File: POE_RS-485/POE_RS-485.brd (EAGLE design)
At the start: 44.5 x 38.1 mm, 9 parts, among them IC1 7805

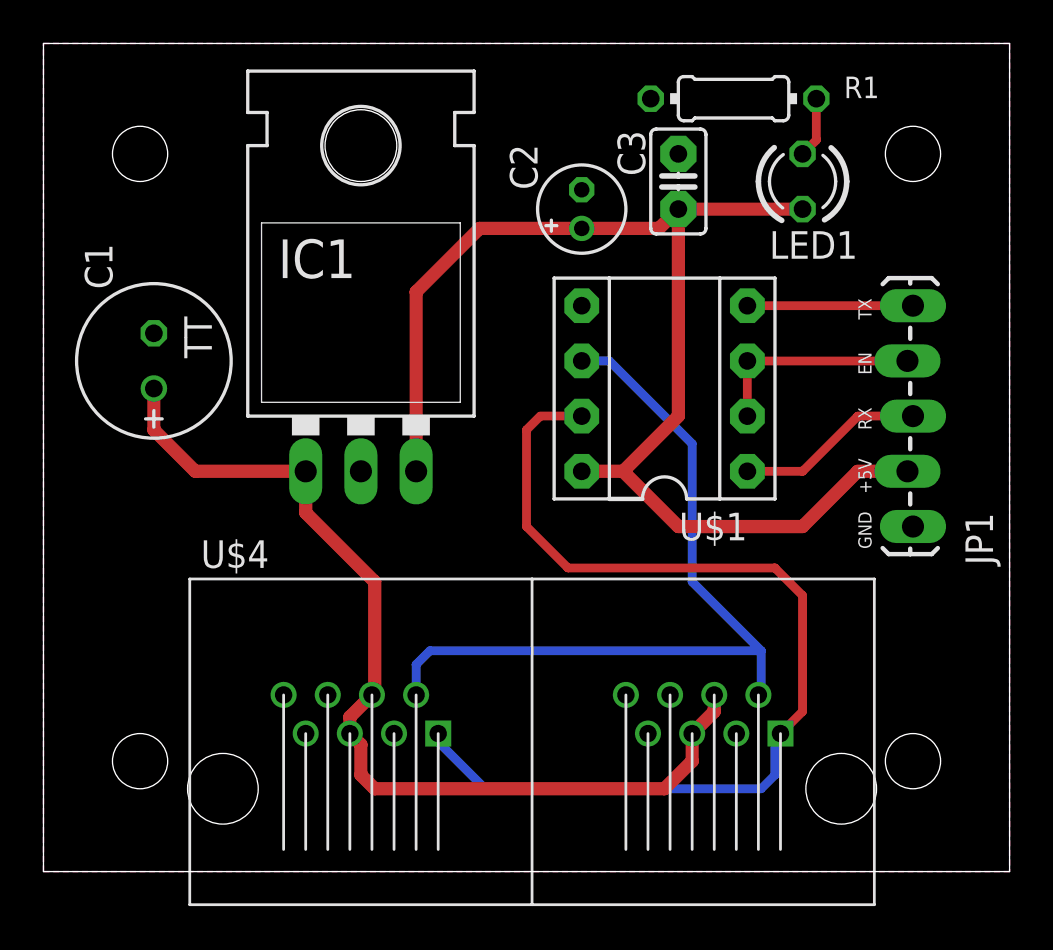
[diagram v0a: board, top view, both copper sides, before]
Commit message: Hot tub fill monitor: added
other updates
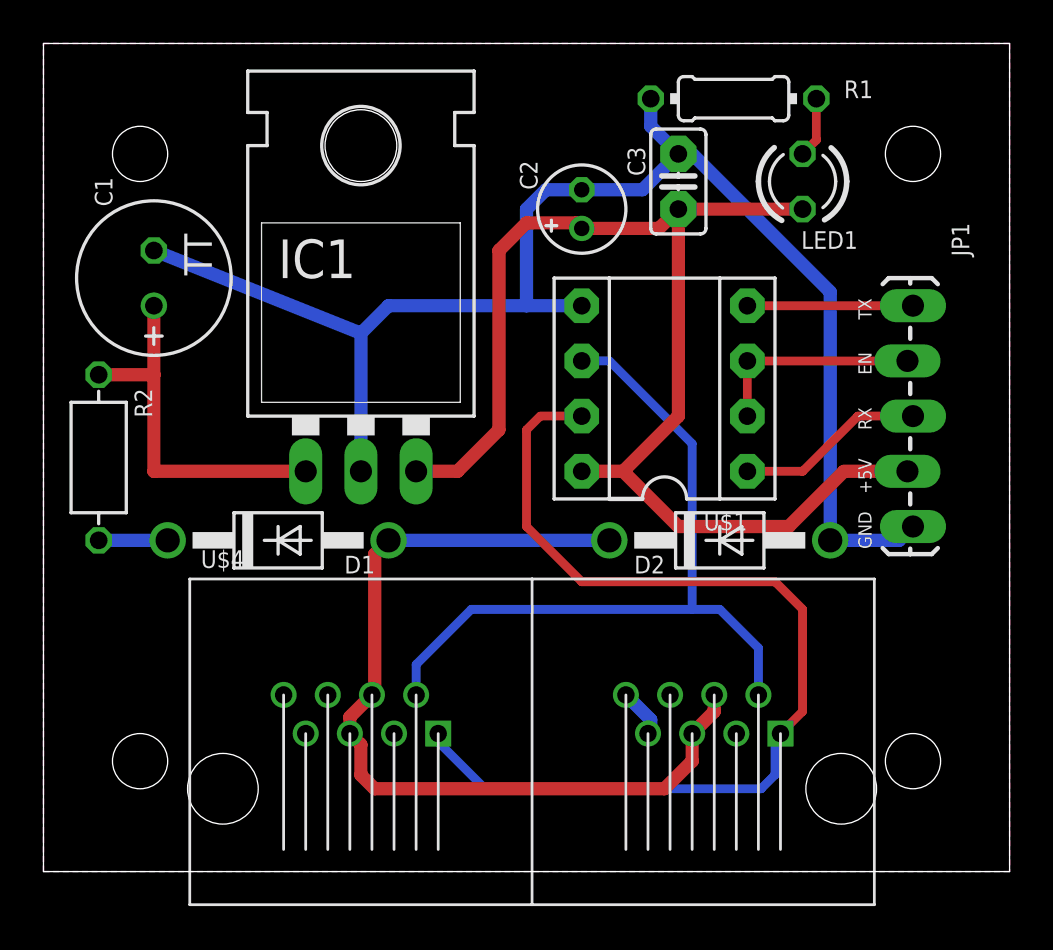
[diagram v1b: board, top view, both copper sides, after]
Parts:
- added D1, D2: 1N4004, diode:DO41-10
- added R2: THERMISTOR-7,5, varistor:R-7,5
- R1: value 330R -> 560R
- moved C1 3.81 mm to (5.08, 27.3)
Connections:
- new net N$3: C1.+, IC1.IN, R2.1
- new net N$4: D1.C, R2.2
- net GND: now also D2.A
- net VIN: now also D1.A, D2.C; no longer C1.+, IC1.IN
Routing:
- net GND: track 0.00 -> 70.3 mm
- net N$3: track 0.00 -> 17.1 mm
- net VIN: track 45.1 -> 41.4 mm
- net N$4: track 0.00 -> 3.17 mm
- net B_BLUE: track 37.1 -> 35.4 mm
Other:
- board text added: "POE_RS-485 v1.2"
- board text removed: "POE_RS-485 v1.1"
